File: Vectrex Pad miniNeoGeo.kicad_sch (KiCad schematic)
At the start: 28 parts, among them J1 DB9_Female, SW1 SW_Push, SW2 SW_Push, SW3 SW_Push, SW4 SW_Push, SW5 SW_DP3T, SW6 SW_DP3T, U1 NE555D, U2 74LVC2G00, U3 74LVC2G32

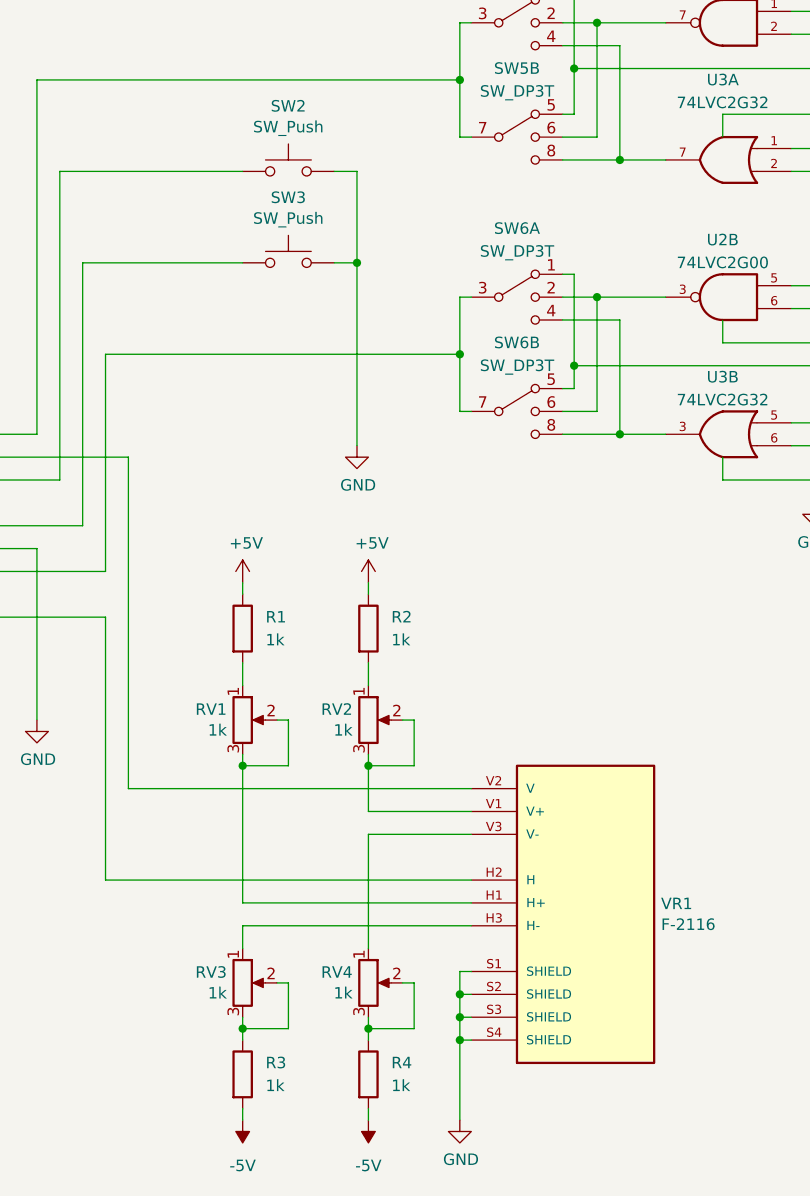
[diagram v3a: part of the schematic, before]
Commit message: Replace 1k resistor with 470
The value of the resistors for the sensitivity of the analog pad is too high. Test with 470 ohms.
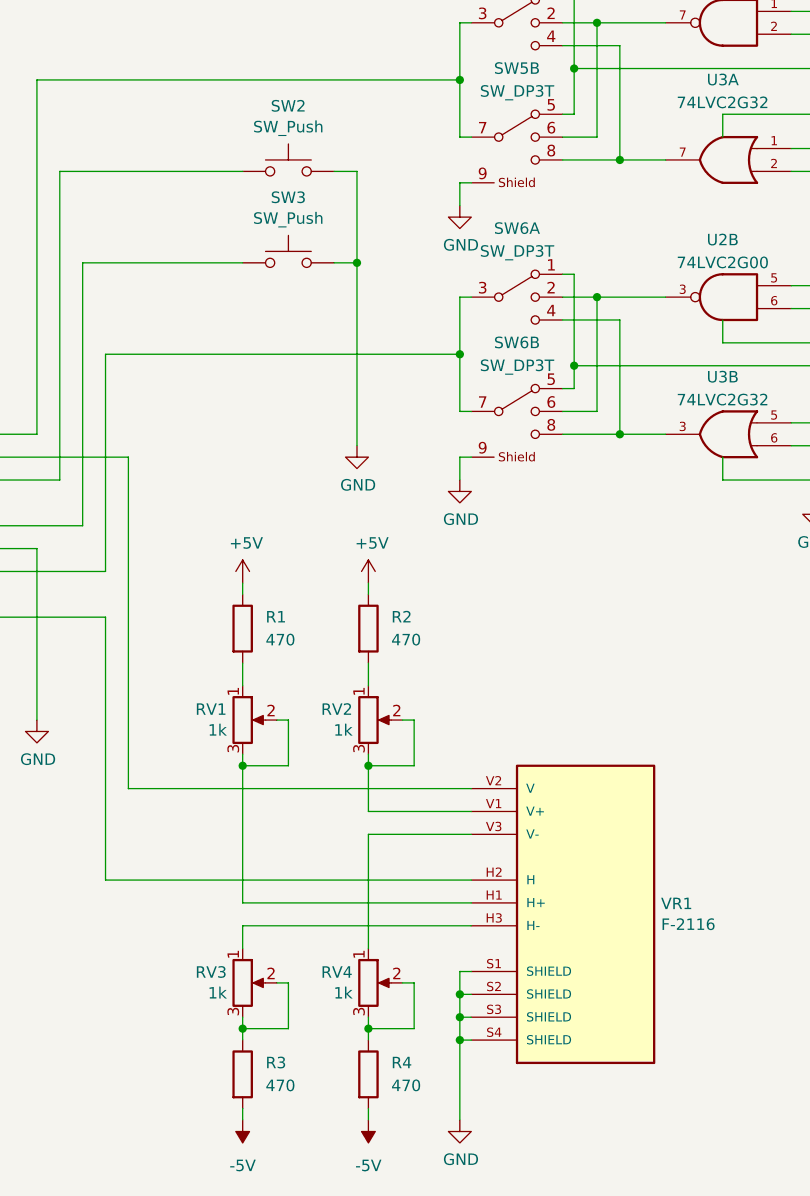
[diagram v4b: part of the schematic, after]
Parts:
- R1, R2, R3, R4: value 1k -> 470
- SW5, SW6: symbol Switch:SW_DP3T -> Vextrec miniNeoGeo:OS203011MS1QP1
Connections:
- net GND: now also SW5.9 (Shield), SW6.9 (Shield)
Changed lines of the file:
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@@
+    (stroke (width 0) (type default) (color 0 0 0 0))
+  )
+  (wire (pts (xy 124.46 66.04) (xy 123.19 66.04))
     (stroke (width 0) (type default) (color 0 0 0 0))
   )
@@
     (stroke (width 0) (type default) (color 0 0 0 0))
   )
+  (wire (pts (xy 124.46 96.52) (xy 123.19 96.52))
+    (stroke (width 0) (type default) (color 0 0 0 0))
+  )
   (wire (pts (xy 78.74 99.06) (xy 78.74 64.77))
     (stroke (width 0) (type default) (color 0 0 0 0))
@@
     (stroke (width 0) (type default) (color 0 0 0 0))
   )
+  (wire (pts (xy 123.19 96.52) (xy 123.19 99.06))
+    (stroke (width 0) (type default) (color 0 0 0 0))
+  )
   (wire (pts (xy 212.09 90.17) (xy 212.09 92.71))
     (stroke (width 0) (type default) (color 0 0 0 0))
@@
   )
   (wire (pts (xy 140.97 81.28) (xy 140.97 93.98))
+    (stroke (width 0) (type default) (color 0 0 0 0))
+  )
+  (wire (pts (xy 123.19 66.04) (xy 123.19 68.58))
     (stroke (width 0) (type default) (color 0 0 0 0))
   )
@@
     (pin "2")
   )
-  (symbol (lib_id "Switch:SW_DP3T") (at 129.54 91.44 0) (unit 2)
+  (symbol (lib_id "power:GND") (at 123.19 99.06 0) (unit 1)
+    (in_bom yes) (on_board yes)
+    (property "Reference" "#PWR?" (id 0) (at 123.19 105.41 0)
+      (effects (font (size 1.27 1.27)) hide)
+    )
+    (property "Value" "GND" (id 1) (at 123.317 103.4542 0))
+    (property "Footprint" "" (id 2) (at 123.19 99.06 0)
+      (effects (font (size 1.27 1.27)) hide)
+    )
+    (property "Datasheet" "" (id 3) (at 123.19 99.06 0)
+      (effects (font (size 1.27 1.27)) hide)
+    )
+    (pin "1")
+  )
+  (symbol (lib_name "OS203011MS1QP1_2") (lib_id "Vextrec miniNeoGeo:OS203011MS1QP1") (at 129.54 91.44 0) (unit 2)
     (in_bom yes) (on_board yes) (fields_autoplaced)
     (property "Reference" "SW6" (id 0) (at 129.54 83.82 0))
     (property "Value" "SW_DP3T" (id 1) (at 129.54 86.36 0))
-    (property "Footprint" "Vectrex Pad miniNeoGeo:OS203011MS1QP1" (id 2) (at 113.665 86.995 0)
+    (property "Footprint" "Vectrex Pad miniNeoGeo:OS203011MS1QP1" (id 2) (at 129.54 86.36 0)
       (effects (font (size 1.27 1.27)) hide)
     )
@@
     (pin "7")
     (pin "8")
+    (pin "9")
   )
   (symbol (lib_id "power:+5V") (at 181.61 26.67 0) (unit 1)
@@
       (effects (font (size 1.27 1.27)) (justify left))
     )
-    (property "Value" "1k" (id 1) (at 101.6 116.8399 0)
+    (property "Value" "470" (id 1) (at 101.6 116.8399 0)
       (effects (font (size 1.27 1.27)) (justify left))
     )
@@
     (pin "2")
   )
-  (symbol (lib_id "Switch:SW_DP3T") (at 129.54 60.96 0) (unit 2)
+  (symbol (lib_name "OS203011MS1QP1_3") (lib_id "Vextrec miniNeoGeo:OS203011MS1QP1") (at 129.54 60.96 0) (unit 2)
     (in_bom yes) (on_board yes) (fields_autoplaced)
     (property "Reference" "SW5" (id 0) (at 129.54 53.34 0))
     (property "Value" "SW_DP3T" (id 1) (at 129.54 55.88 0))
-    (property "Footprint" "Vectrex Pad miniNeoGeo:OS203011MS1QP1" (id 2) (at 113.665 56.515 0)
+    (property "Footprint" "Vectrex Pad miniNeoGeo:OS203011MS1QP1" (id 2) (at 129.54 55.88 0)
       (effects (font (size 1.27 1.27)) hide)
     )
@@
     (pin "7")
     (pin "8")
+    (pin "9")
   )
   (symbol (lib_id "power:GND") (at 198.12 95.25 0) (unit 1)
@@
     )
     (property "Datasheet" "" (id 3) (at 198.12 95.25 0)
+      (effects (font (size 1.27 1.27)) hide)
+    )
+    (pin "1")
+  )
+  (symbol (lib_id "power:GND") (at 123.19 68.58 0) (unit 1)
+    (in_bom yes) (on_board yes)
+    (property "Reference" "#PWR?" (id 0) (at 123.19 74.93 0)
+      (effects (font (size 1.27 1.27)) hide)
+    )
+    (property "Value" "GND" (id 1) (at 123.317 72.9742 0))
+    (property "Footprint" "" (id 2) (at 123.19 68.58 0)
+      (effects (font (size 1.27 1.27)) hide)
+    )
+    (property "Datasheet" "" (id 3) (at 123.19 68.58 0)
       (effects (font (size 1.27 1.27)) hide)
     )
@@
     (pin "6")
   )
-  (symbol (lib_id "Switch:SW_DP3T") (at 129.54 78.74 0) (unit 1)
+  (symbol (lib_name "OS203011MS1QP1_1") (lib_id "Vextrec miniNeoGeo:OS203011MS1QP1") (at 129.54 78.74 0) (unit 1)
     (in_bom yes) (on_board yes) (fields_autoplaced)
     (property "Reference" "SW6" (id 0) (at 129.54 71.12 0))
     (property "Value" "SW_DP3T" (id 1) (at 129.54 73.66 0))
-    (property "Footprint" "Vectrex Pad miniNeoGeo:OS203011MS1QP1" (id 2) (at 113.665 74.295 0)
+    (property "Footprint" "Vectrex Pad miniNeoGeo:OS203011MS1QP1" (id 2) (at 129.54 73.66 0)
       (effects (font (size 1.27 1.27)) hide)
     )
@@
       (effects (font (size 1.27 1.27)) (justify left))
     )
-    (property "Value" "1k" (id 1) (at 115.57 166.3699 0)
+    (property "Value" "470" (id 1) (at 115.57 166.3699 0)
       (effects (font (size 1.27 1.27)) (justify left))
     )
@@
       (effects (font (size 1.27 1.27)) (justify left))
     )
-    (property "Value" "1k" (id 1) (at 115.57 116.8399 0)
+    (property "Value" "470" (id 1) (at 115.57 116.8399 0)
       (effects (font (size 1.27 1.27)) (justify left))
     )
@@
       (effects (font (size 1.27 1.27)) (justify left))
     )
-    (property "Value" "1k" (id 1) (at 101.6 166.3699 0)
+    (property "Value" "470" (id 1) (at 101.6 166.3699 0)
       (effects (font (size 1.27 1.27)) (justify left))
     )
@@
     (pin "2")
   )
-  (symbol (lib_id "Switch:SW_DP3T") (at 129.54 48.26 0) (unit 1)
+  (symbol (lib_id "Vextrec miniNeoGeo:OS203011MS1QP1") (at 129.54 48.26 0) (unit 1)
     (in_bom yes) (on_board yes) (fields_autoplaced)
     (property "Reference" "SW5" (id 0) (at 129.54 40.64 0))
     (property "Value" "SW_DP3T" (id 1) (at 129.54 43.18 0))
-    (property "Footprint" "Vectrex Pad miniNeoGeo:OS203011MS1QP1" (id 2) (at 113.665 43.815 0)
+    (property "Footprint" "Vectrex Pad miniNeoGeo:OS203011MS1QP1" (id 2) (at 129.54 43.18 0)
       (effects (font (size 1.27 1.27)) hide)
     )
@@
       (reference "#PWR0122") (unit 1) (value "GND") (footprint "")
     )
+    (path "/373e38ec-419c-4a25-bb4e-22a9ec751438"
+      (reference "#PWR?") (unit 1) (value "GND") (footprint "")
+    )
+    (path "/93f6fda8-57a1-4f54-9916-ca04ad5f8ae1"
+      (reference "#PWR?") (unit 1) (value "GND") (footprint "")
+    )
     (path "/00000000-0000-0000-0000-000061b5a283"
       (reference "C2") (unit 1) (value "10nF") (footprint "Capacitor_SMD:C_0805_2012Metric")
@@
     )
     (path "/671384fa-6255-470c-b133-72c2ad3c497f"
-      (reference "R1") (unit 1) (value "1k") (footprint "Resistor_SMD:R_0805_2012Metric")
+      (reference "R1") (unit 1) (value "470") (footprint "Resistor_SMD:R_0805_2012Metric")
     )
     (path "/d14dbe84-d61d-4866-bff5-09cd08533de4"
-      (reference "R2") (unit 1) (value "1k") (footprint "Resistor_SMD:R_0805_2012Metric")
+      (reference "R2") (unit 1) (value "470") (footprint "Resistor_SMD:R_0805_2012Metric")
     )
     (path "/f8f03543-8f6e-4cac-9306-1c2001611295"
-      (reference "R3") (unit 1) (value "1k") (footprint "Resistor_SMD:R_0805_2012Metric")
+      (reference "R3") (unit 1) (value "470") (footprint "Resistor_SMD:R_0805_2012Metric")
     )
     (path "/b0a35062-c6cd-4fd6-8c7f-d92fb5c5eb06"
-      (reference "R4") (unit 1) (value "1k") (footprint "Resistor_SMD:R_0805_2012Metric")
+      (reference "R4") (unit 1) (value "470") (footprint "Resistor_SMD:R_0805_2012Metric")
     )
     (path "/abfc8cbb-01a5-4624-8ace-917245035b98"

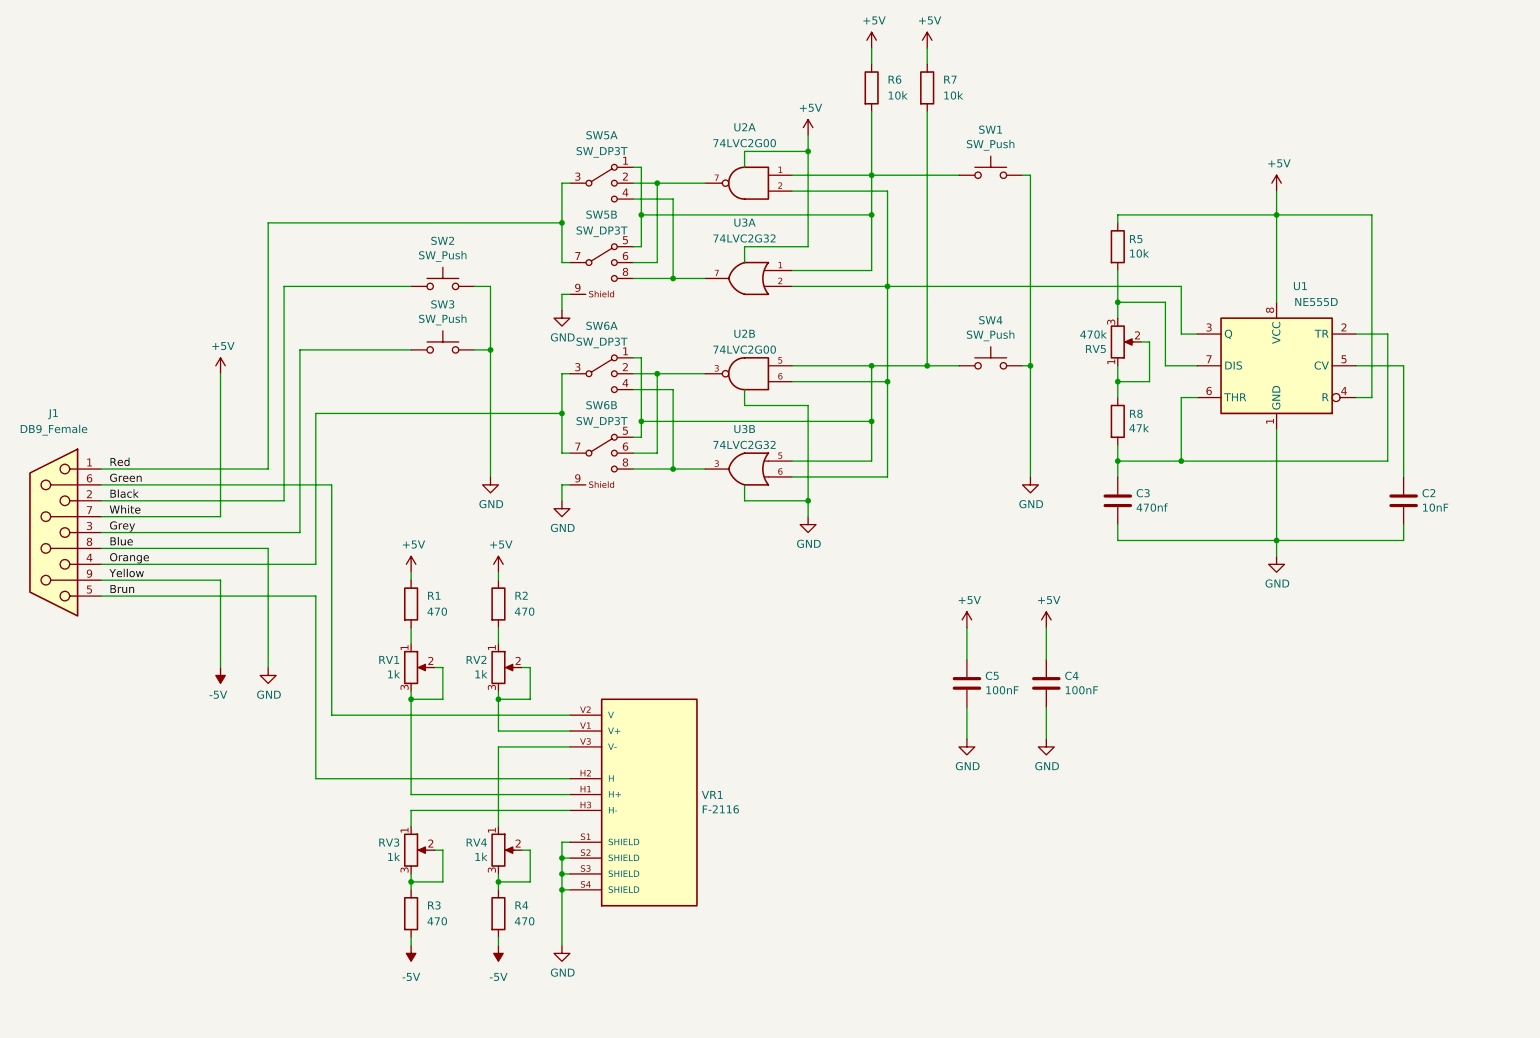
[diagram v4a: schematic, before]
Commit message: Correct issue #1
Because of the resistance of the silicone contacts, it is necessary to press hard on the buttons to make the contact.
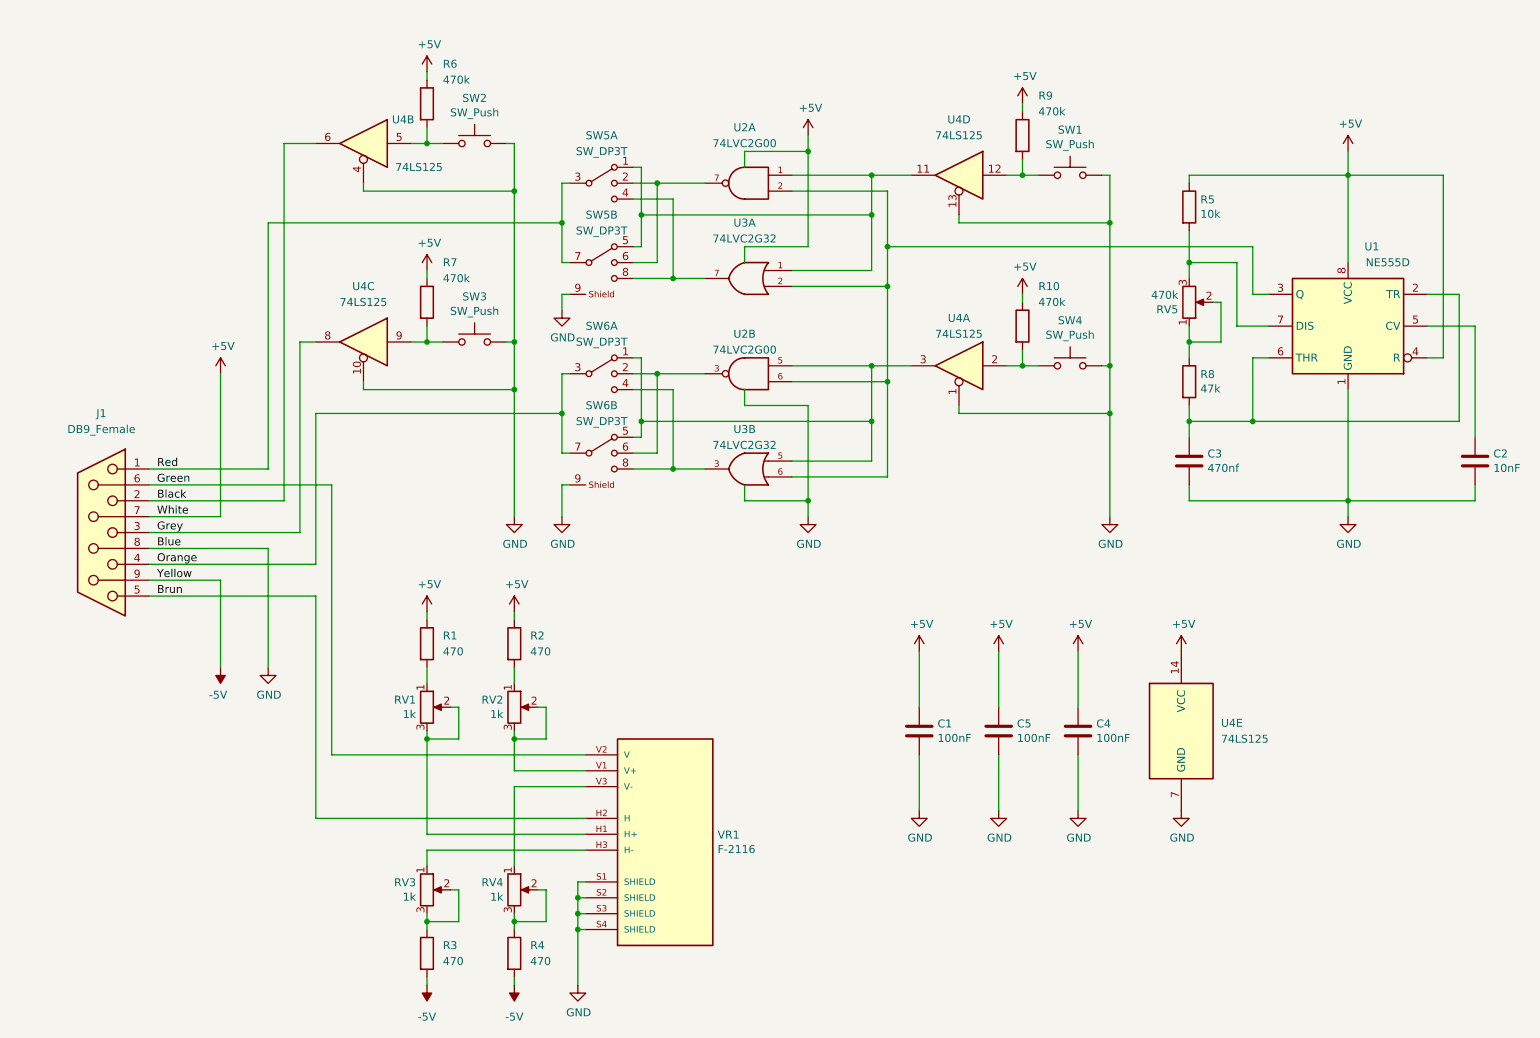
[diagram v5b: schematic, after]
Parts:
- added C1: 100nF, Capacitor_SMD:C_0805_2012Metric, symbol Device:C
- added R10, R9: 470k, Resistor_SMD:R_0805_2012Metric, symbol Device:R
- added U4: 74LS125, Package_SO:TSSOP-14_4.4x5mm_P0.65mm, symbol 74xx:74LS125
- R6, R7: value 10k -> 470k
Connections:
- net +5V: now also C1.1, R10.1, R9.1, U4.14 (VCC)
- net Black: now also U4.6; no longer SW2.1
- net GND: now also C1.2, U4.1, U4.10, U4.13, U4.4, U4.7 (GND)
- net Grey: now also U4.8; no longer SW3.1
- net at SW6.1, SW6.5, U2.5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: now also U4.3; no longer R7.2, SW4.1
- net at SW5.1, SW5.5, U2.1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: now also U4.11; no longer R6.2, SW1.1
- new net: R7.2, SW3.1, U4.9
- new net: R6.2, SW2.1, U4.5
- new net: R10.2, SW4.1, U4.2
- new net: R9.2, SW1.1, U4.12
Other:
- moved on the sheet: C2, C3, C4, C5, J1, R1, R2, R3, R4, R5, R6, R7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

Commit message: Suppression of redundant potentiometers
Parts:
- removed RV3, RV4: 1k, Potentiometer_THT:Potentiometer_ACP_CA9-V10_Vertical_Hole, symbol Device:R_POT
- R1, R2: value 470 -> 330
- R3, R4: value 470 -> 820
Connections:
- net at VR1.H3 (H-): now also R3.1
- net at VR1.V3 (V-): now also R4.1
